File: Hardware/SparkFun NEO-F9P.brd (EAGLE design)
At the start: 43.2 x 43.2 mm, 129 parts, among them J1 ANTENNA-SMA-GROUNDEDEDGE_SMA, J2 Qwiic Right Angle, J4 Qwiic Right Angle, U1 U-BLOX_NEO-F9P-15B, U2 3.3V

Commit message: Add LNA_EN label
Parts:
- added U$67: (no value), output:#LNA_EN#0
- moved U$43 1.92 mm to (35.6, 30.5)
- moved PWR\1 1.90 mm to (37.5, 30.5)
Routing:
- net RTK_STAT: track 45.1 -> 43.1 mm
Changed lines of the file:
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@@
 <layer number="47" name="Measures" color="7" fill="1" visible="no" active="yes"/>
 <layer number="48" name="Document" color="7" fill="1" visible="no" active="yes"/>
-<layer number="49" name="Reference" color="13" fill="1" visible="yes" active="yes"/>
+<layer number="49" name="Reference" color="13" fill="1" visible="no" active="yes"/>
 <layer number="50" name="dxf" color="7" fill="1" visible="no" active="yes"/>
 <layer number="51" name="tDocu" color="6" fill="1" visible="yes" active="yes"/>
@@
 <attribute name="VALUE" x="40.64" y="35.56" size="0.6096" layer="27" font="vector" ratio="20" align="top-center"/>
 </element>
-<element name="PWR\1" library="SparkFun-Jumpers" package="SMT-JUMPER_2_NC_TRACE_SILK" package3d_urn="urn:adsk.eagle:package:39281/1" value="JUMPER-SMT_2_NC_TRACE_SILK" x="39.37" y="30.48" smashed="yes" rot="MR0">
-<attribute name="NAME" x="39.37" y="31.623" size="0.6096" layer="26" font="vector" ratio="20" rot="MR0" align="bottom-center"/>
-<attribute name="VALUE" x="39.37" y="29.337" size="0.6096" layer="28" font="vector" ratio="20" rot="MR0" align="top-center"/>
+<element name="PWR\1" library="SparkFun-Jumpers" package="SMT-JUMPER_2_NC_TRACE_SILK" package3d_urn="urn:adsk.eagle:package:39281/1" value="JUMPER-SMT_2_NC_TRACE_SILK" x="37.465" y="30.48" smashed="yes" rot="MR0">
+<attribute name="NAME" x="37.465" y="31.623" size="0.6096" layer="26" font="vector" ratio="20" rot="MR0" align="bottom-center"/>
+<attribute name="VALUE" x="37.465" y="29.337" size="0.6096" layer="28" font="vector" ratio="20" rot="MR0" align="top-center"/>
 </element>
 <element name="U$14" library="output" package="#RTK_STAT#0" value="" x="29.21" y="36.195" smashed="yes" rot="R90"/>
@@
 <element name="U$55" library="output" package="##SB##0" value="" x="29.21" y="14.732" smashed="yes" rot="MR270"/>
 <element name="U$62" library="output" package="#PULSE#0" value="" x="31.75" y="16.129" smashed="yes" rot="MR270"/>
-<element name="U$43" library="output" package="#RTK#0" value="" x="37.465" y="30.226" smashed="yes" rot="MR270"/>
+<element name="U$43" library="output" package="#RTK#0" value="" x="35.56" y="30.48" smashed="yes" rot="MR270"/>
 <element name="TP1" library="SparkFun-Connectors" package="1X01_NO_SILK" value="TEST-POINTPOGO_PTH" x="29.21" y="12.7" smashed="yes">
 <attribute name="NAME" x="27.94" y="13.843" size="0.6096" layer="25" font="vector" ratio="20"/>
@@
 <element name="U$66" library="output" package="RECEIVER0" value="" x="24.13" y="21.59" smashed="yes" rot="MR270"/>
 <element name="LOGO1" library="SparkFun-Aesthetics" package="ORDERING_INSTRUCTIONS" value="SPECIAL_INSTRUCTIONS-ORDERING" x="54.61" y="50.8" smashed="yes"/>
+<element name="U$67" library="output" package="#LNA_EN#0" value="" x="11.43" y="33.401" smashed="yes" rot="MR270"/>
 </elements>
 <signals>
@@
 <wire x1="25.146" y1="30.226" x2="29.21" y2="34.29" width="0.1524" layer="16"/>
 <wire x1="29.21" y1="34.29" x2="29.21" y2="41.91" width="0.1524" layer="16"/>
-<wire x1="38.8493" y1="30.48" x2="32.766" y2="30.48" width="0.1524" layer="16"/>
+<wire x1="36.9443" y1="30.48" x2="32.766" y2="30.48" width="0.1524" layer="16"/>
 <wire x1="30.988" y1="28.702" x2="25.146" y2="28.702" width="0.1524" layer="16"/>
 <wire x1="32.766" y1="30.48" x2="30.988" y2="28.702" width="0.1524" layer="16"/>
@@
 <contactref element="PWR\1" pad="1"/>
 <contactref element="R17" pad="2"/>
-<via x="42.545" y="30.48" extent="1-16" drill="0.3"/>
-<wire x1="39.8907" y1="30.48" x2="42.545" y2="30.48" width="0.1524" layer="16"/>
-<wire x1="41.49" y1="34.29" x2="41.49" y2="31.535" width="0.1524" layer="1"/>
-<wire x1="41.49" y1="31.535" x2="42.545" y2="30.48" width="0.1524" layer="1"/>
+<via x="41.275" y="33.02" extent="1-16" drill="0.3"/>
+<wire x1="41.275" y1="33.02" x2="41.275" y2="31.2293" width="0.1524" layer="16"/>
+<wire x1="41.275" y1="31.2293" x2="40.5257" y2="30.48" width="0.1524" layer="16"/>
+<wire x1="40.5257" y1="30.48" x2="37.9857" y2="30.48" width="0.1524" layer="16"/>
+<wire x1="41.49" y1="34.29" x2="41.49" y2="33.235" width="0.1524" layer="1"/>
+<wire x1="41.49" y1="33.235" x2="41.275" y2="33.02" width="0.1524" layer="1"/>
 </signal>
 <signal name="LNA_EN">

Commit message: Add backup batt. Add PPS LED and PTH. Change silk. Fix RTK LED.
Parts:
- removed J8: (no value), SparkFun-Connectors:1X09_NO_SILK
- removed LOGO6: QWIIC_LOGO_5MM, SparkFun-Aesthetics:QWIIC_5MM
- removed TP3: TEST-POINTPOGO_PTH, SparkFun-Connectors:1X01_NO_SILK
- removed U$1: (no value), output:#GND#0
- removed U$62: (no value), output:#PULSE#0
- added B1: 6.8MM_COIN_CELL, SparkFun-Batteries:ML414H_IV01E
- added C8: 1.0uF, SparkFun-Capacitors:0603
- added D3: 0.5A/40V/420mV, SparkFun-DiscreteSemi:SOD-323
- added D6: Yellow, SparkFun-LED:LED-0603
- added J6: (no value), SparkFun-Connectors:1X10_NO_SILK
- added PULSE: JUMPER-SMT_2_NC_TRACE_SILK, SparkFun-Jumpers:SMT-JUMPER_2_NC_TRACE_SILK
- added R18: 1k, SparkFun-Resistors:0603
- added R19: 2.2k, SparkFun-Resistors:0603@1
- added U$68: (no value), output:PPS0
- added U$69: (no value), output:#PPS#0
- added U$70: (no value), output:#_PPS#0
- added U$71: (no value), output:#PPS_#0
- added U$72: (no value), output:##SAFE##0
- C1, C5, C7: device SparkFun-Capacitors:0603 -> SparkFun-Capacitors:0603@1
- D4: value RED -> Red
- D5: value RED -> Blue
- LOGO3: value SFE_LOGO_NAME_FLAME.1_INCH -> SFE_LOGO_NAME_FLAME7_MM; device SparkFun-Aesthetics:SFE_LOGO_NAME_FLAME_.1 -> SparkFun-Aesthetics:SFE_LOGO_NAME_FLAME_7MM
- R10, R11, R12, R13, R14, R15, R16, R2, R3, R4, R5, R6, R7, R8, R9: device SparkFun-Resistors:0603 -> SparkFun-Resistors:0603@1
- R17: value 1k -> 2.2k; device SparkFun-Resistors:0603 -> SparkFun-Resistors:0603@1
- U$55: device output:##SB##0 -> output:#G#0
- moved TP2 26.2 mm to (11.4, 29.2)
- moved U$55 19.1 mm to (14.0, 3.17), flipped to the top, turned to 90 degrees
- moved U$61 6.35 mm to (36.8, 15.2)
- moved LOGO3 5.88 mm to (34.9, 15.1)
- moved R12 0.92 mm to (3.81, 6.99)
- moved R13 0.92 mm to (3.81, 18.4)
- moved C2 0.51 mm to (17.4, 9.14)
- moved C4 0.51 mm to (23.0, 9.14)
- moved C5 0.51 mm to (24.6, 9.14)
- moved U2 0.36 mm to (20.3, 9.14)
- renumbered LED1 to D4, LED2 to D5, PWR\1 to RTK
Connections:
- new net BACKUP: B1.+, C8.1, R18.1, U1.22
- new net N$20: D3.C, R18.2
- new net N$21: D6.A, R19.1
- new net N$22: PULSE.1, R19.2
- net 3.3V: now also D3.A, J6.3, RTK.2; no longer J8.3, U1.22
- net 5V: now also J6.2; no longer J8.2
- net GND: now also B1.-, C8.2, D6.C, J6.1; no longer D5.C, J8.1
- net LNA_EN: now also TP2.1; no longer TP3.1
- net PULSE: now also J6.10, PULSE.2; no longer TP2.1
- net RTK_STAT: now also D5.C; no longer RTK.2
- net RXD1/PICO: now also J6.8; no longer J8.8
- net RXD2: now also J6.4; no longer J8.4
- net SCL/SCK: now also J6.9; no longer J8.9
- net SDA/!CS!: now also J6.6; no longer J8.6
- net TXD1/POCI: now also J6.7; no longer J8.7
- net TXD2: now also J6.5; no longer J8.5
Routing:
- net 3.3V: track 139.4 -> 157.0 mm, vias 3 -> 8
- net PULSE: track 2.08 -> 19.1 mm, vias 0 -> 3
- net BACKUP: track 0.00 -> 13.2 mm, vias 0 -> 2
- net GND: track 30.7 -> 20.9 mm, vias 148 -> 133
- net N$9: track 7.76 -> 13.5 mm, vias 0 -> 2
- net 5V: track 38.8 -> 44.1 mm, vias 2 -> 3
- net N$22: track 0.00 -> 3.31 mm, vias 0 -> 1
- net N$7: track 7.60 -> 10.6 mm
- net N$20: track 0.00 -> 2.68 mm
- net N$21: track 0.00 -> 2.62 mm
- net SDA/!CS!: track 119.4 -> 117.7 mm
- net RTK_STAT: track 43.1 -> 44.3 mm, vias 1 -> 2
- net SCL/SCK: track 126.8 -> 125.8 mm
- net TXD2: track 67.1 -> 66.3 mm
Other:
- board text added: "N. Seidle"
- board text removed: "Paul Clark"

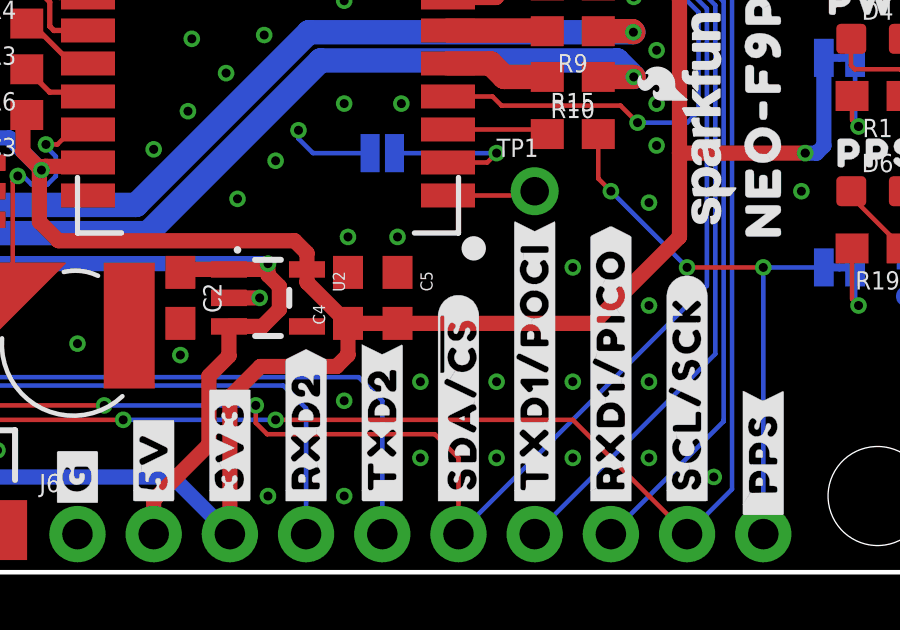
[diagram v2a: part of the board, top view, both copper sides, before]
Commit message: Move R2.
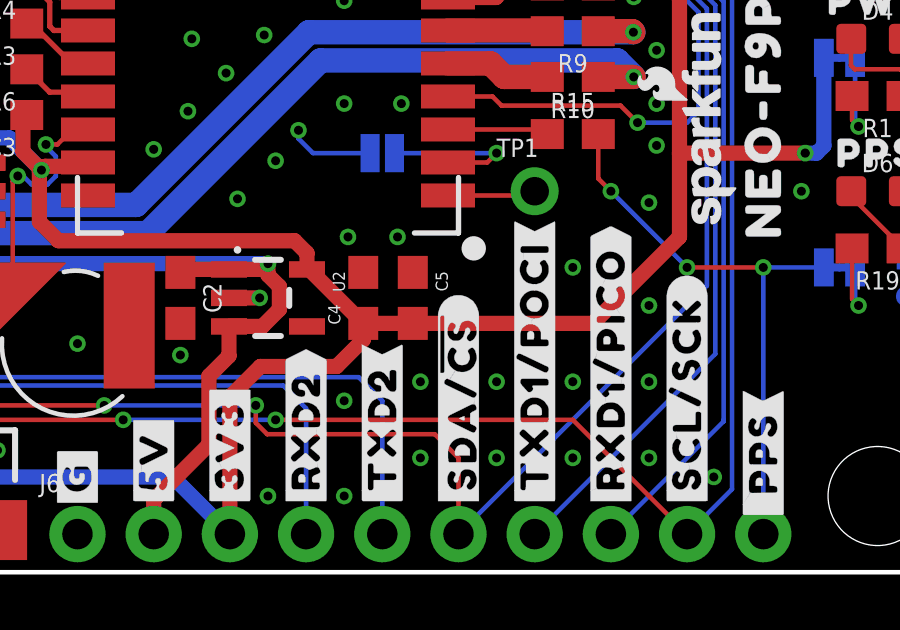
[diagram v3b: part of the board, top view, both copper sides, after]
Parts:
- moved C4 0.51 mm to (23.5, 9.14)
- moved C5 0.51 mm to (25.1, 9.14)
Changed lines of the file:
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@@
 <element name="JP91" library="SparkFun" package="STAND-OFF" value="STAND-OFF" x="2.54" y="2.54" smashed="yes"/>
 <element name="JP101" library="SparkFun" package="STAND-OFF" value="STAND-OFF" x="40.64" y="2.54" smashed="yes"/>
-<element name="C4" library="SparkFun-Capacitors" package="0603" value="1.0uF" x="22.987" y="9.144" smashed="yes" rot="R90">
-<attribute name="NAME" x="22.225" y="8.255" size="0.4064" layer="25" font="vector" rot="R90"/>
-<attribute name="PROD_ID" value="CAP-00868" x="22.987" y="9.144" size="1.778" layer="27" rot="R90" display="off"/>
-<attribute name="VALUE" value="1.0uF" x="22.86" y="7.747" size="0.4064" layer="27" font="vector" rot="R270"/>
-</element>
-<element name="C5" library="SparkFun-Capacitors" package="0603@1" value="0.1uF" x="24.638" y="9.144" smashed="yes" rot="R270">
-<attribute name="NAME" x="25.4" y="10.033" size="0.4064" layer="25" font="vector" rot="R270"/>
-<attribute name="PROD_ID" value="CAP-00810" x="24.638" y="9.144" size="1.778" layer="27" rot="R270" display="off"/>
-<attribute name="VALUE" value="0.1uF" x="25.273" y="10.16" size="0.4064" layer="27" font="vector" rot="R270"/>
+<element name="C4" library="SparkFun-Capacitors" package="0603" value="1.0uF" x="23.495" y="9.144" smashed="yes" rot="R90">
+<attribute name="NAME" x="22.733" y="8.255" size="0.4064" layer="25" font="vector" rot="R90"/>
+<attribute name="PROD_ID" value="CAP-00868" x="23.495" y="9.144" size="1.778" layer="27" rot="R90" display="off"/>
+<attribute name="VALUE" value="1.0uF" x="23.368" y="7.747" size="0.4064" layer="27" font="vector" rot="R270"/>
+</element>
+<element name="C5" library="SparkFun-Capacitors" package="0603@1" value="0.1uF" x="25.146" y="9.144" smashed="yes" rot="R270">
+<attribute name="NAME" x="25.908" y="10.033" size="0.4064" layer="25" font="vector" rot="R270"/>
+<attribute name="PROD_ID" value="CAP-00810" x="25.146" y="9.144" size="1.778" layer="27" rot="R270" display="off"/>
+<attribute name="VALUE" value="0.1uF" x="25.781" y="10.16" size="0.4064" layer="27" font="vector" rot="R270"/>
 </element>
 <element name="D4" library="SparkFun-LED" package="LED-0603" value="Red" x="40.64" y="17.78" smashed="yes">
@@
 <contactref element="PWR\" pad="2"/>
 <wire x1="13.335" y1="11.049" x2="21.209" y2="11.049" width="0.508" layer="1"/>
-<wire x1="24.638" y1="8.294" x2="22.987" y2="8.294" width="0.508" layer="1"/>
+<wire x1="25.146" y1="8.294" x2="23.495" y2="8.294" width="0.508" layer="1"/>
 <wire x1="9.39" y1="38.1" x2="9.39" y2="39.616" width="0.508" layer="1"/>
 <wire x1="9.39" y1="39.616" x2="10.033" y2="40.259" width="0.508" layer="1"/>
@@
 <contactref element="RTK" pad="2"/>
 <wire x1="19.05" y1="1.27" x2="19.05" y2="5.842" width="0.508" layer="1"/>
-<wire x1="21.6201" y1="10.094" x2="21.6201" y2="9.6609" width="0.508" layer="1"/>
-<wire x1="22.987" y1="8.294" x2="21.6201" y2="9.6609" width="0.508" layer="1"/>
+<wire x1="23.495" y1="8.294" x2="21.695" y2="10.094" width="0.508" layer="1"/>
+<wire x1="21.6201" y1="10.094" x2="21.695" y2="10.094" width="0.508" layer="1"/>
 <wire x1="8.39" y1="5.08" x2="8.39" y2="6.208" width="0.508" layer="1"/>
 <wire x1="8.39" y1="6.208" x2="7.74" y2="6.858" width="0.508" layer="1"/>
 <wire x1="21.6201" y1="10.6379" x2="21.6201" y2="10.094" width="0.508" layer="1"/>
 <wire x1="21.209" y1="11.049" x2="21.6201" y2="10.6379" width="0.508" layer="1"/>
-<wire x1="24.638" y1="8.294" x2="31.154" y2="8.294" width="0.508" layer="1"/>
+<wire x1="25.146" y1="8.294" x2="31.154" y2="8.294" width="0.508" layer="1"/>
 <wire x1="12.28" y1="15.24" x2="12.153" y2="15.113" width="0.508" layer="1"/>
 <wire x1="12.153" y1="15.113" x2="12.153" y2="14.02" width="0.508" layer="1"/>
@@
 <wire x1="8.89" y1="3.175" x2="17.145" y2="3.175" width="0.508" layer="16"/>
 <wire x1="17.145" y1="3.175" x2="19.05" y2="1.27" width="0.508" layer="16"/>
-<wire x1="22.606" y1="6.858" x2="22.987" y2="7.239" width="0.508" layer="1"/>
-<wire x1="22.987" y1="7.239" x2="22.987" y2="8.294" width="0.508" layer="1"/>
+<wire x1="22.606" y1="6.858" x2="23.495" y2="7.747" width="0.508" layer="1"/>
+<wire x1="23.495" y1="7.747" x2="23.495" y2="8.294" width="0.508" layer="1"/>
 <wire x1="20.066" y1="6.858" x2="22.606" y2="6.858" width="0.508" layer="1"/>
 <via x="26.67" y="30.48" extent="1-16" drill="0.3"/>

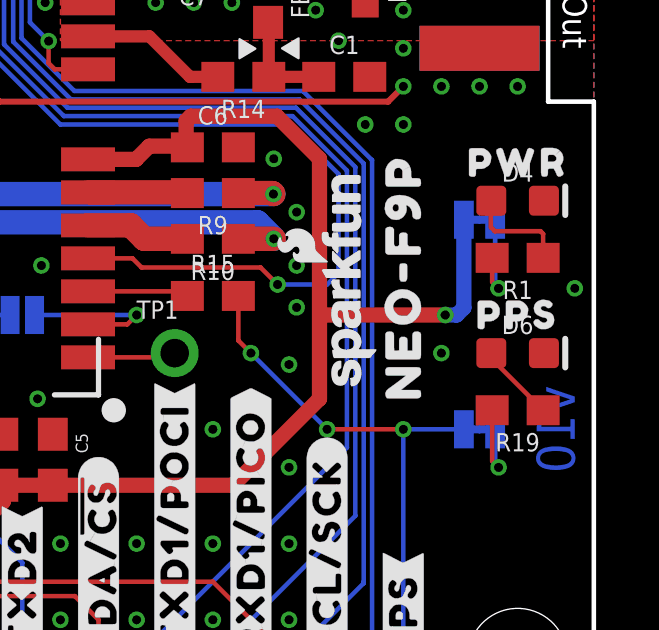
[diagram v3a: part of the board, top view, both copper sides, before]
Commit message: Adjust layout post design review.
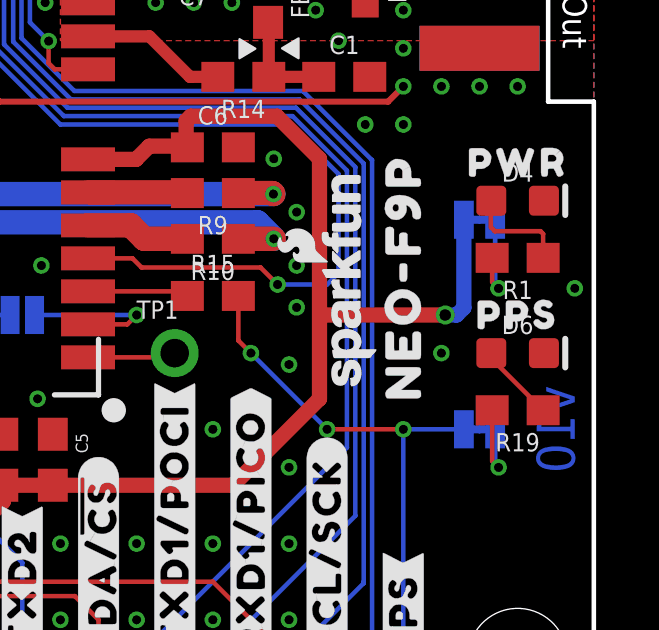
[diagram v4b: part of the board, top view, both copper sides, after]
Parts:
- C1, C5, C7: device SparkFun-Capacitors:0603@1 -> SparkFun-Capacitors:0603
- R10, R11, R12, R13, R14, R15, R16, R17, R19, R2, R3, R4, R5, R6, R7, R8, R9: device SparkFun-Resistors:0603@1 -> SparkFun-Resistors:0603

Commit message: Increase version to v11
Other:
- board text added: "v11"
- board text removed: "v10"
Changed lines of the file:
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@@
 <wire x1="43.18" y1="21.082" x2="43.18" y2="0" width="0.1524" layer="20"/>
 <wire x1="43.18" y1="0" x2="0" y2="0" width="0.1524" layer="20"/>
-<text x="41.91" y="10.16" size="1.27" layer="16" font="vector" ratio="15" rot="SMR270" align="center">v10</text>
+<text x="41.91" y="10.16" size="1.27" layer="16" font="vector" ratio="15" rot="SMR270" align="center">v11</text>
 <text x="33.02" y="-7.62" size="1.778" layer="47" font="vector" ratio="15" align="bottom-center">Measurements in inches</text>
 <dimension x1="0" y1="0" x2="0" y2="43.18" x3="-10.16" y3="21.59" textsize="1.778" textratio="15" layer="47" dtype="vertical" unit="inch"/>
